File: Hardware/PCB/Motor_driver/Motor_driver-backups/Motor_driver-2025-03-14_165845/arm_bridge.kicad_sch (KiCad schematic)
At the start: 9 parts

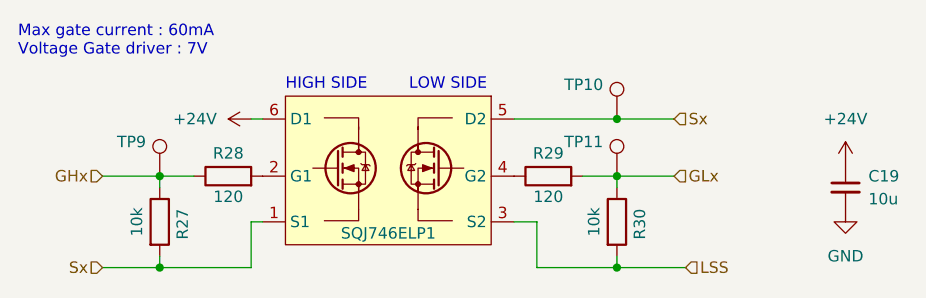
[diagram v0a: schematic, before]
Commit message: update schematic
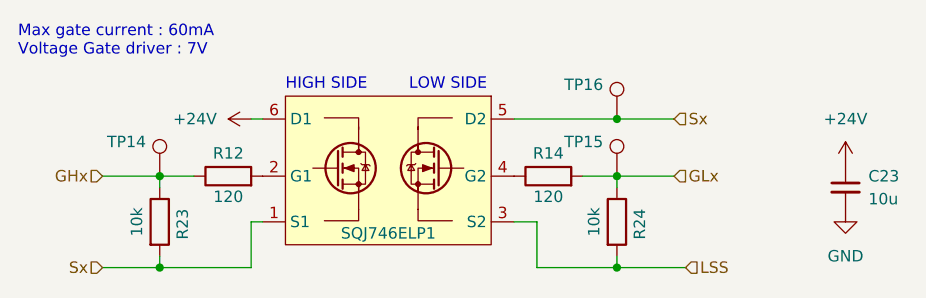
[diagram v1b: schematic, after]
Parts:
- TP14: renamed from TP9; footprint TestPoint:TestPoint_Pad_D1.0mm -> TestPoint:TestPoint_Pad_D1.5mm
- TP15: renamed from TP11; footprint TestPoint:TestPoint_Pad_D1.0mm -> TestPoint:TestPoint_Pad_D1.5mm
- TP16: renamed from TP10; footprint TestPoint:TestPoint_Pad_D1.0mm -> TestPoint:TestPoint_Pad_D1.5mm
- renumbered C19 to C23, R28 to R12, R29 to R14, R27 to R23, R30 to R24
